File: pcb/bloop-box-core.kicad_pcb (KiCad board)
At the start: 4 copper layers, 65 x 30 mm, 34 parts, among them J1 Raspberry_Pi_Header, J2 USB_C_Receptacle_USB2.0_16P, J4 Micro_SD_Card_Det1, SW1 Reset, SW2 Boot, U1 ESP32-C5-WROOM-1U, U2 AMS1117-3.3, U3 74LVC125APW

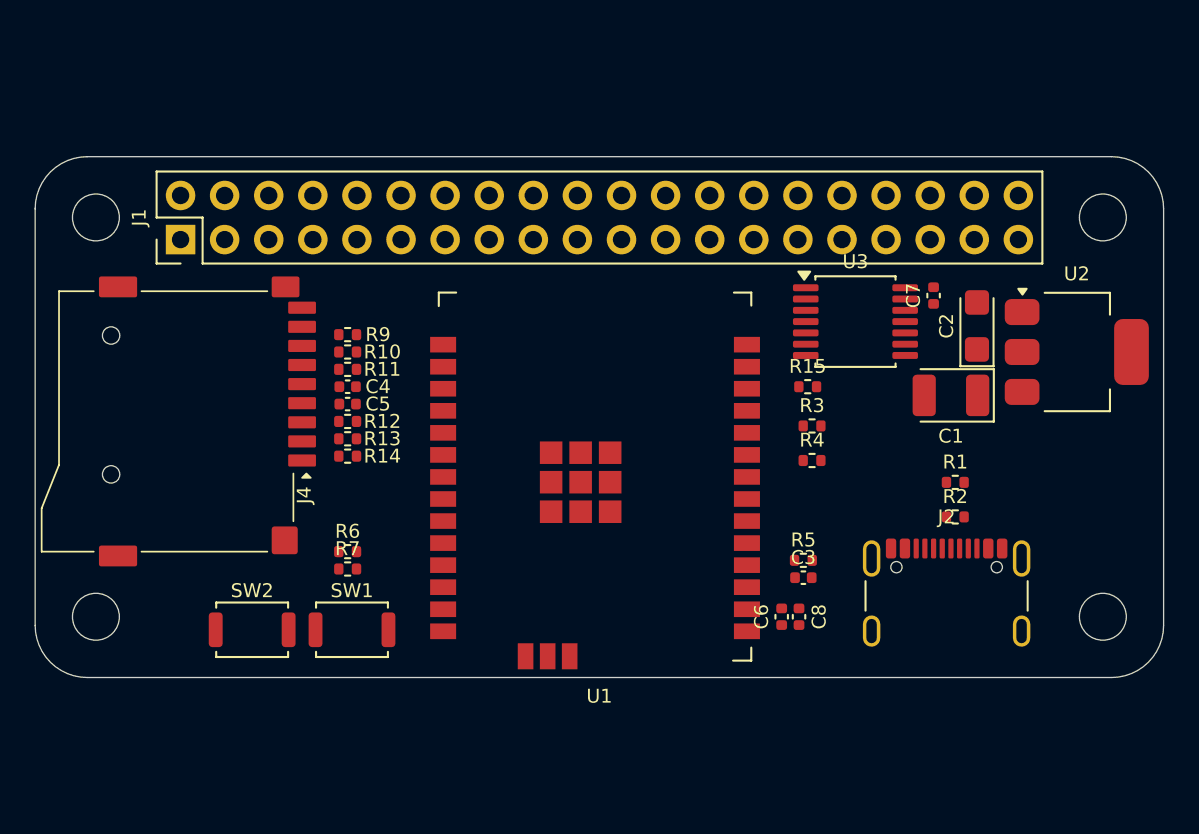
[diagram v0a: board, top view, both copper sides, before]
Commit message: feat: trace-routing
All traces are routed
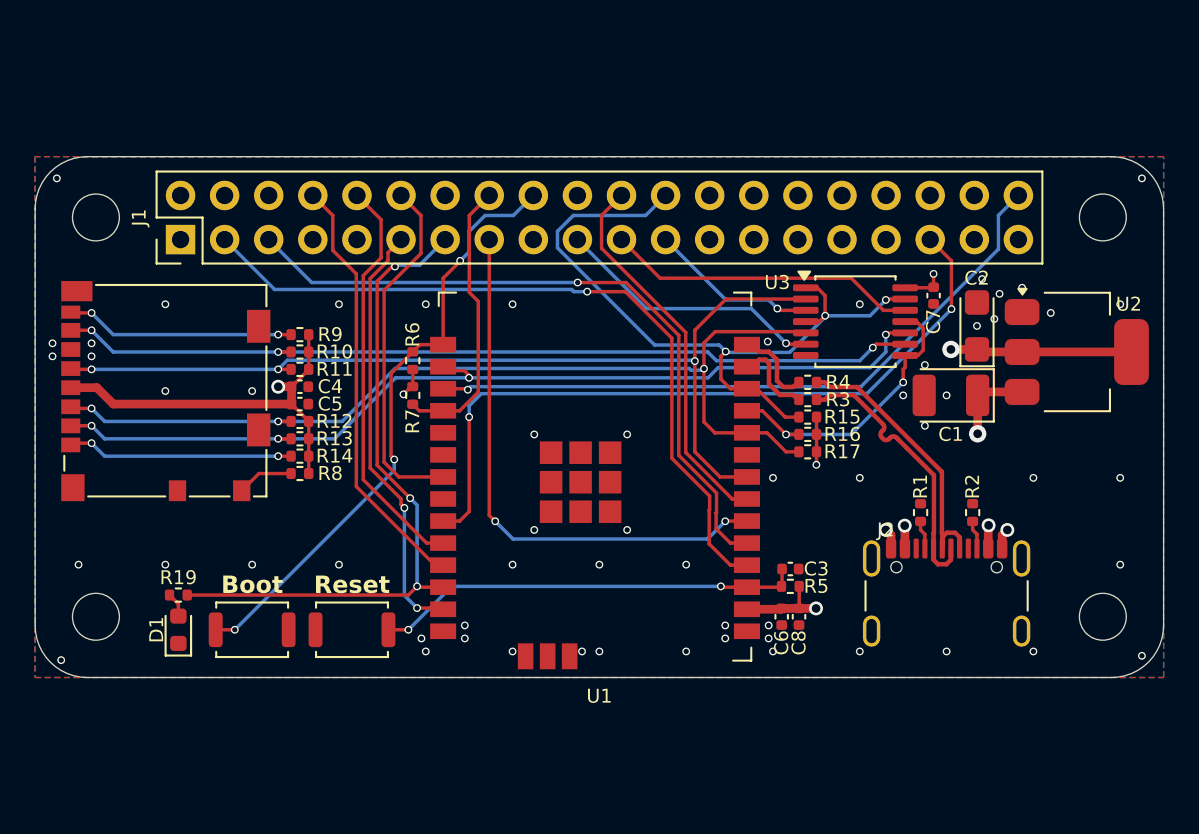
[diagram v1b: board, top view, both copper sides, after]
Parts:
- added D1: ACT, LED_SMD:LED_0603_1608Metric, F.Cu at (125.8, 93.8)
- added R16: 10k, Resistor_SMD:R_0402_1005Metric, F.Cu at (162.0, 82.5)
- added R17: 10k, Resistor_SMD:R_0402_1005Metric, F.Cu at (162.0, 83.5)
- added R19: 1k, Resistor_SMD:R_0402_1005Metric, F.Cu at (125.8, 91.8)
- added R8: 100k, Resistor_SMD:R_0402_1005Metric, F.Cu at (132.8, 84.8)
- J2: value USB_C_Receptacle_USB2.0_16P -> USB_C
- J4: value Micro_SD_Card_Det1 -> Micro_SD_Card_Det2; footprint My_Footprints:TF_PUSH_Micro-SD-Connector -> Connector_Card:microSD_HC_Molex_104031-0811
- moved R6 11.6 mm to (139.2, 78.2), turned to 90 degrees
- moved R7 10.7 mm to (139.2, 80.2), turned to -90 degrees
- moved R4 4.51 mm to (162.0, 79.5), turned to 180 degrees
- moved J4 3.58 mm to (125.0, 80.0), turned to 90 degrees
- moved C4 2.75 mm to (132.8, 79.8)
- moved C5 2.75 mm to (132.8, 80.8)
- moved R10 2.75 mm to (132.8, 77.8)
- moved R11 2.75 mm to (132.8, 78.8)
- moved R12 2.75 mm to (132.8, 81.8)
- moved R13 2.75 mm to (132.8, 82.8)
- moved R14 2.75 mm to (132.8, 83.8)
- moved R9 2.75 mm to (132.8, 76.8)
- moved R1 2.65 mm to (168.5, 87.0), turned to 90 degrees
- moved R15 1.75 mm to (162.0, 81.5), turned to 180 degrees
- moved R5 1.68 mm to (161.0, 91.2), turned to 180 degrees
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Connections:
- J1 pad 29: /GPIO5 -> unconnected-(J1-GCLK1/GPIO5-Pad29)
- J1 pad 31: /GPIO6 -> unconnected-(J1-GCLK2/GPIO6-Pad31)
- J4 pad 10: GND -> /SD_DETECT
- J4 pad 9: unconnected-(J4-DET-Pad9) -> GND
- U3 pad 10: /NFC_Select -> /SD_Select
- U3 pad 12: /SD_MISO -> /NFC_MISO
- U3 pad 13: /SD_Select -> /NFC_Select
- U3 pad 2: /NFC_MISO -> /SPI_SCK
- U3 pad 3: /SPI_MISO -> /NFC_SCK
- U3 pad 8: /NFC_SCK -> /SPI_MISO
- U3 pad 9: /SPI_SCK -> /SD_MISO
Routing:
- net /SPI_MOSI: track 0.00 -> 55.8 mm, vias 0 -> 3
- net /SPI_SCK: track 0.00 -> 54.7 mm, vias 0 -> 3
- net /SD_Select: track 0.00 -> 54.1 mm, vias 0 -> 4
- net /SD_MISO: track 0.00 -> 49.9 mm, vias 0 -> 3
- net +3V3: track 0.00 -> 45.3 mm, vias 0 -> 6
- net /SDA: track 0.00 -> 43.6 mm, vias 0 -> 1
- net /NFC_Select: track 0.00 -> 42.7 mm, vias 0 -> 3
- net /AMP_LRCLK: track 0.00 -> 42.4 mm, vias 0 -> 2
- net /SCL: track 0.00 -> 40.1 mm, vias 0 -> 1
- net /AMP_DIN: track 0.00 -> 38.9 mm, vias 0 -> 1
- net /Tail_LED1: track 0.00 -> 38.5 mm, vias 0 -> 3
- net /Button1: track 0.00 -> 35.1 mm, vias 0 -> 3
- net /NFC_IRQ: track 0.00 -> 31.7 mm, vias 0 -> 2
- net /EN: track 0.00 -> 24.7 mm, vias 0 -> 2
- net /TX: track 0.00 -> 24.7 mm
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- added copper zone on In2.Cu, net +3V3
- added copper zone on In2.Cu, net +5V
- added copper zone on B.Cu, net GND
- added copper zone on F.Cu, net GND
- added copper zone on In1.Cu, net GND
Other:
- board text added: "Boot"
- board text added: "Reset"

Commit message: feat: add detect pin for SD-Card
connect SD-Detect to IO7

feat: bottom silkscreen
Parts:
- added G***: LOGO, My_Footprints:CutieMark5mmInverted, B.Cu at (137.2, 90.5)
- added REF**: OSHW-Logo_7.5x8mm_SilkScreen, Symbol:OSHW-Logo_7.5x8mm_SilkScreen, B.Cu at (129.0, 91.5)
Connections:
- U1 pad 9: unconnected-(U1-GPIO7-Pad9) -> /SD_DETECT
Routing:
- net /SD_DETECT: track 3.25 -> 30.9 mm, vias 0 -> 2
- net GND: vias 61 -> 68
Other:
- board text added: "${VERSION} ${DATE}"
- board text added: "Bloop Box Core"
- board text added: "qete.sh"

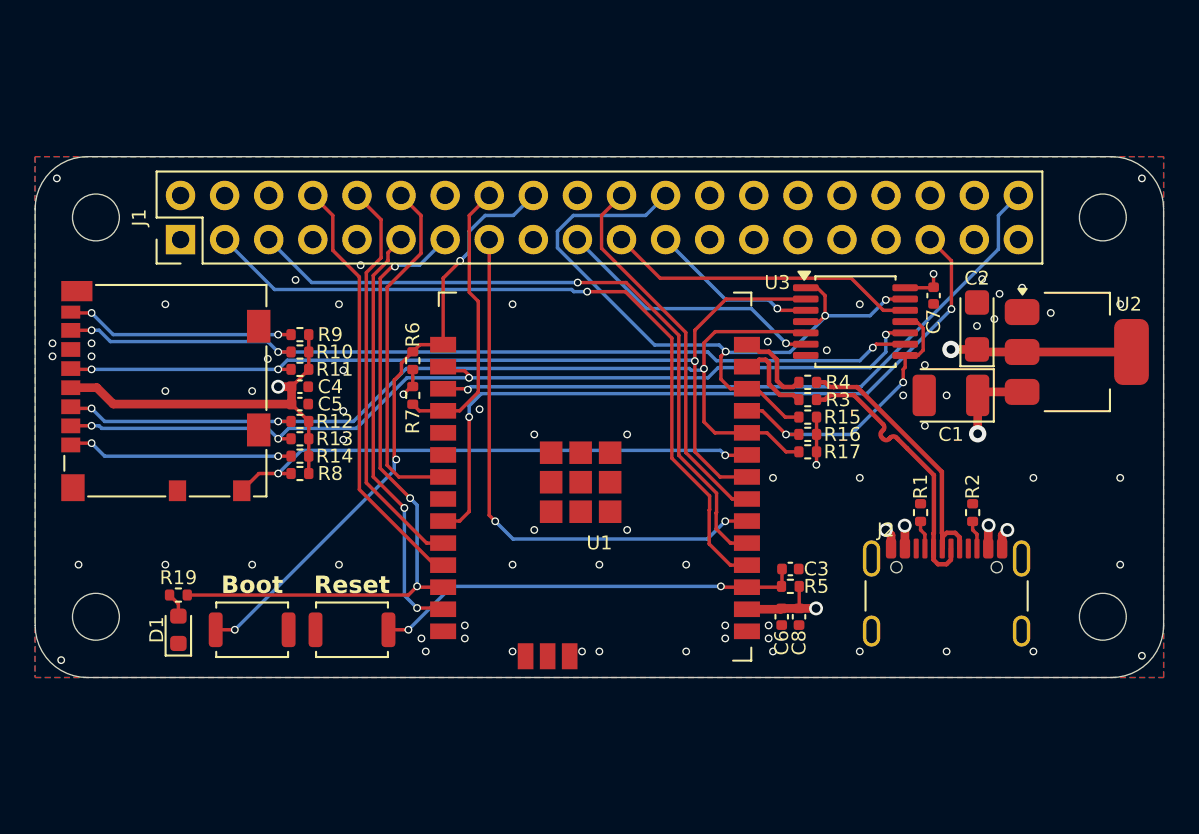
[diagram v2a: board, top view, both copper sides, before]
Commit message: feat: add edge rails
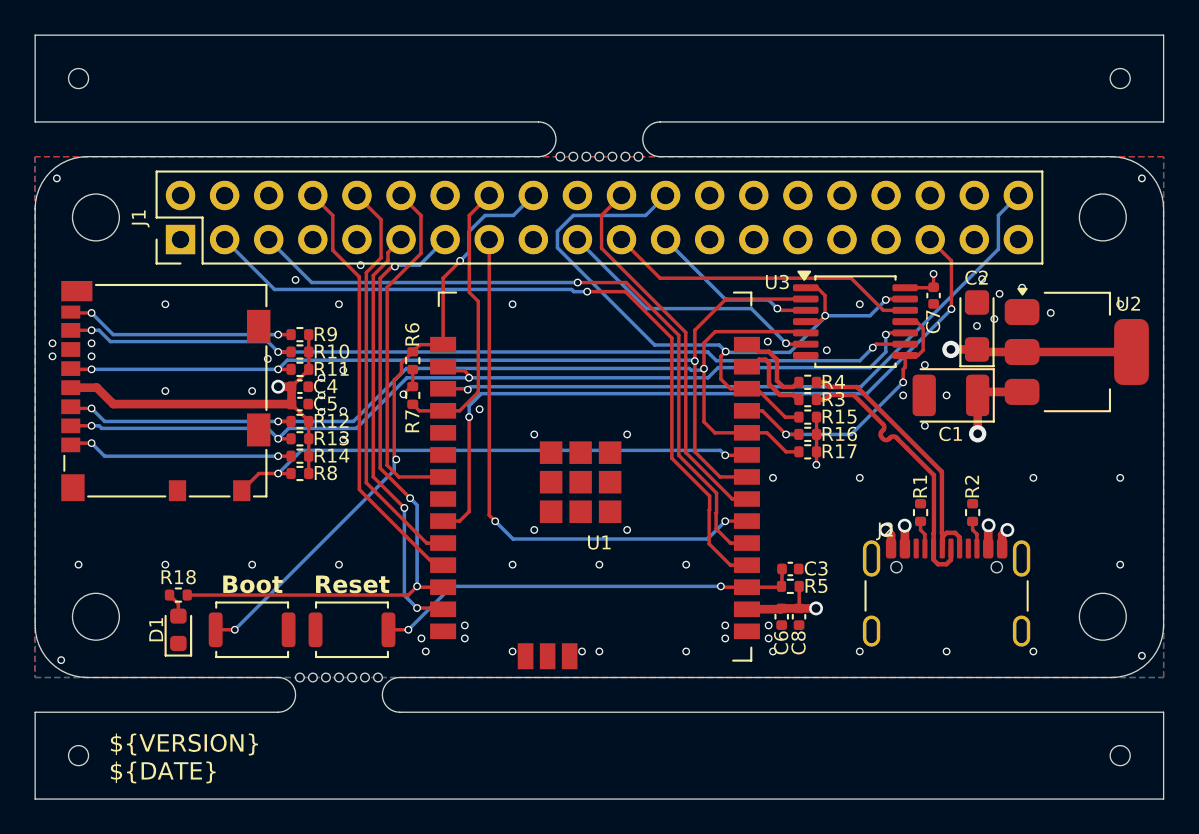
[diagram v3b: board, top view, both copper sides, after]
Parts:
- added REF**: JLCPCB_Tooling_Hole, My_Footprints:JLCPCB_Tooling_Hole, F.Cu at (180.0, 101.0)
- added REF**: JLCPCB_Tooling_Hole, My_Footprints:JLCPCB_Tooling_Hole, F.Cu at (120.0, 101.0)
- added REF**: JLCPCB_Tooling_Hole, My_Footprints:JLCPCB_Tooling_Hole, F.Cu at (180.0, 62.0)
- added REF**: JLCPCB_Tooling_Hole, My_Footprints:JLCPCB_Tooling_Hole, F.Cu at (120.0, 62.0)
- added mouse-bite-2mm-slot: VAL**, Panelization:mouse-bite-2x5mm-slot-onesided-v2, F.Cu at (135.0, 97.5)
- added mouse-bite-2mm-slot: VAL**, Panelization:mouse-bite-2x5mm-slot-onesided-v2, F.Cu at (150.0, 65.5)
- moved G*** 17.0 mm to (154.2, 90.2)
- moved REF** 16.8 mm to (145.8, 91.2)
- renumbered R19 to R18
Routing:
- net GND: vias 68 -> 71
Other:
- board size 65 x 30 mm -> 65 x 44 mm
- board text added: "qete.sh/bloop"

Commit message: fix: capacitor values
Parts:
- moved C1 4.12 mm to (170.8, 80.2), turned to 180 degrees
- moved C2 3.95 mm to (171.5, 76.5), turned to 90 degrees
- moved C4 1.00 mm to (132.8, 80.8)
- moved C5 1.00 mm to (132.8, 79.8)
- moved U2 0.25 mm to (177.8, 77.8)
- renumbered C2 to C1, C1 to C2
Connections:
- C1 pad 1: +3V3 -> +5V
- C2 pad 1: +5V -> +3V3
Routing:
- net /AMP_DIN: track 38.9 -> 40.7 mm
- net /AMP_LRCLK: track 42.4 -> 41.6 mm
- net +3V3: track 45.3 -> 46.2 mm
- net /NFC_Select: track 42.7 -> 43.4 mm
- net +5V: track 7.52 -> 6.90 mm
- net GND: vias 71 -> 89
